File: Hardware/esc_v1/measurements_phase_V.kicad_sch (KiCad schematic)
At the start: 8 parts, among them U10 MAX40056UAUA/V+

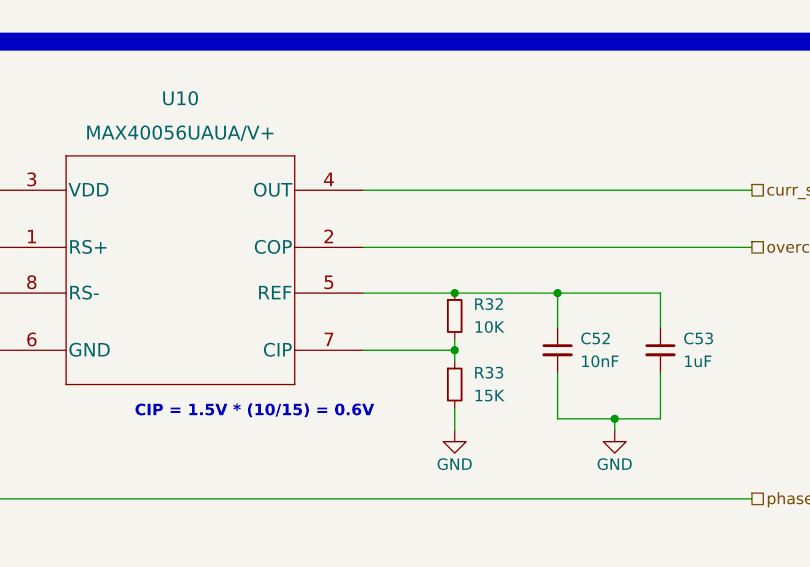
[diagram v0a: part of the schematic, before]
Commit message: changed gate driver, removed 10V buck and 5V LDO, added 5V buck. Started on Layout
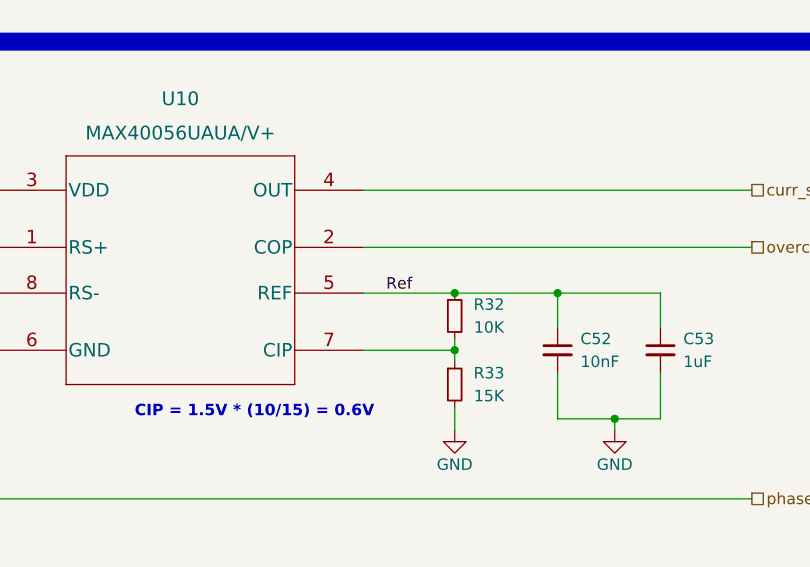
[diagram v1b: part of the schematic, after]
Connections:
- net Ref: now reaches C52.1, C53.1, R32.1, U10.5 (REF)
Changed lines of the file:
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@@
 (kicad_sch (version 20211123) (generator eeschema)
   (paper "A4")
+  (title_block
+    (date "2022-08-13")
+    (rev "1")
+  )
   (junction (at 92.71 80.01) (diameter 0) (color 0 0 0 0)
   )
@@
     (effects (font (size 1.27 1.27) bold) (justify left bottom))
   )
+  (label "Ref" (at 162.56 91.44 0)
+    (effects (font (size 1.27 1.27)) (justify left bottom))
+  )
   (hierarchical_label "3V" (shape passive) (at 76.2 80.01 180)

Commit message: Removed USB to serial chip and added serial connector. Finished layout, made production files and sent to production
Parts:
- R31: Manufacturer_Name (none) -> Vishay
- U10: Manufacturer_Name (none) -> Maxim Integrated; Part no (none) -> MAX40056UAUA/V+
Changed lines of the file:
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@@
       (effects (font (size 1.524 1.524)) hide)
+    )
+    (property "Part no" "MAX40056UAUA/V+" (id 4) (at 119.38 81.28 0)
+      (effects (font (size 1.27 1.27)) hide)
+    )
+    (property "Manufacturer_Name" "Maxim Integrated" (id 5) (at 119.38 81.28 0)
+      (effects (font (size 1.27 1.27)) hide)
     )
     (pin "1")
@@
       (effects (font (size 1.27 1.27)) hide)
     )
+    (property "Manufacturer_Name" "Vishay" (id 6) (at 105.41 114.3 90)
+      (effects (font (size 1.27 1.27)) hide)
+    )
